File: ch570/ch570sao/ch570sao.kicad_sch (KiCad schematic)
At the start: 12 parts, among them J1 SAO, SW1 TS-1187A-B-A-B, SW2 TS-1187A-B-A-B, U2 CH570Q

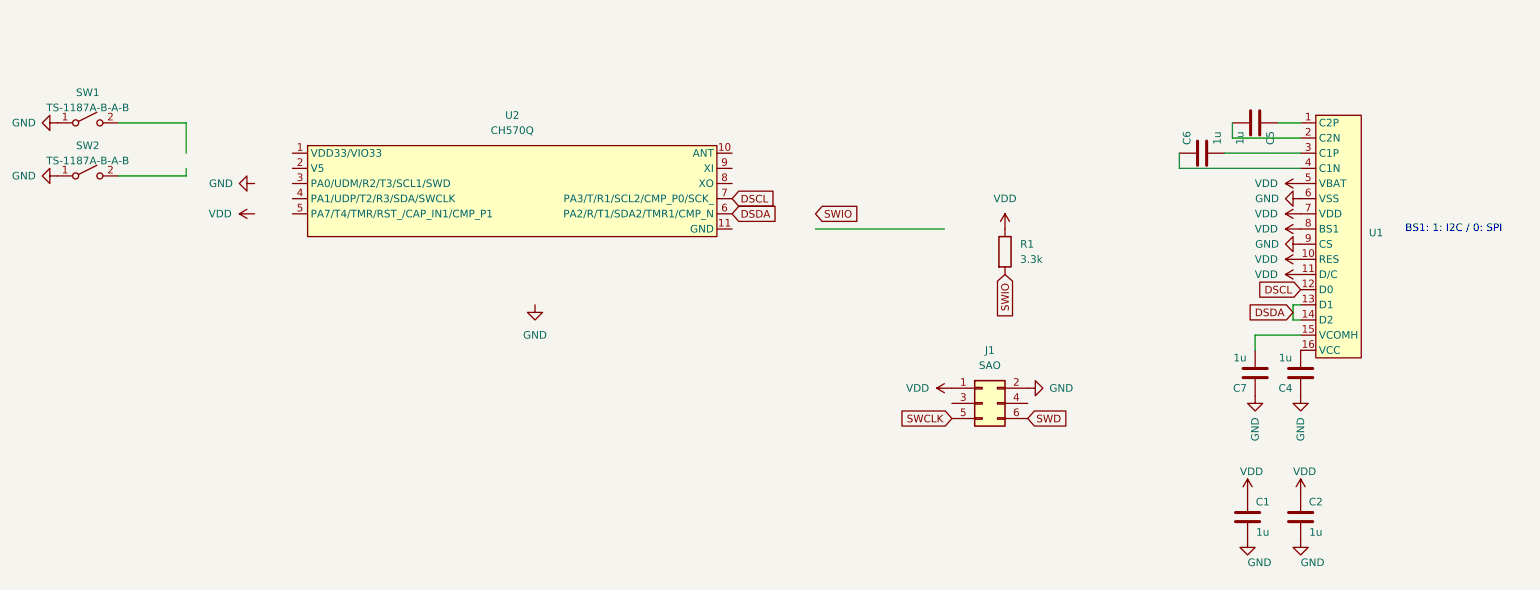
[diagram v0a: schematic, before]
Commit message: Add ch570 saob test
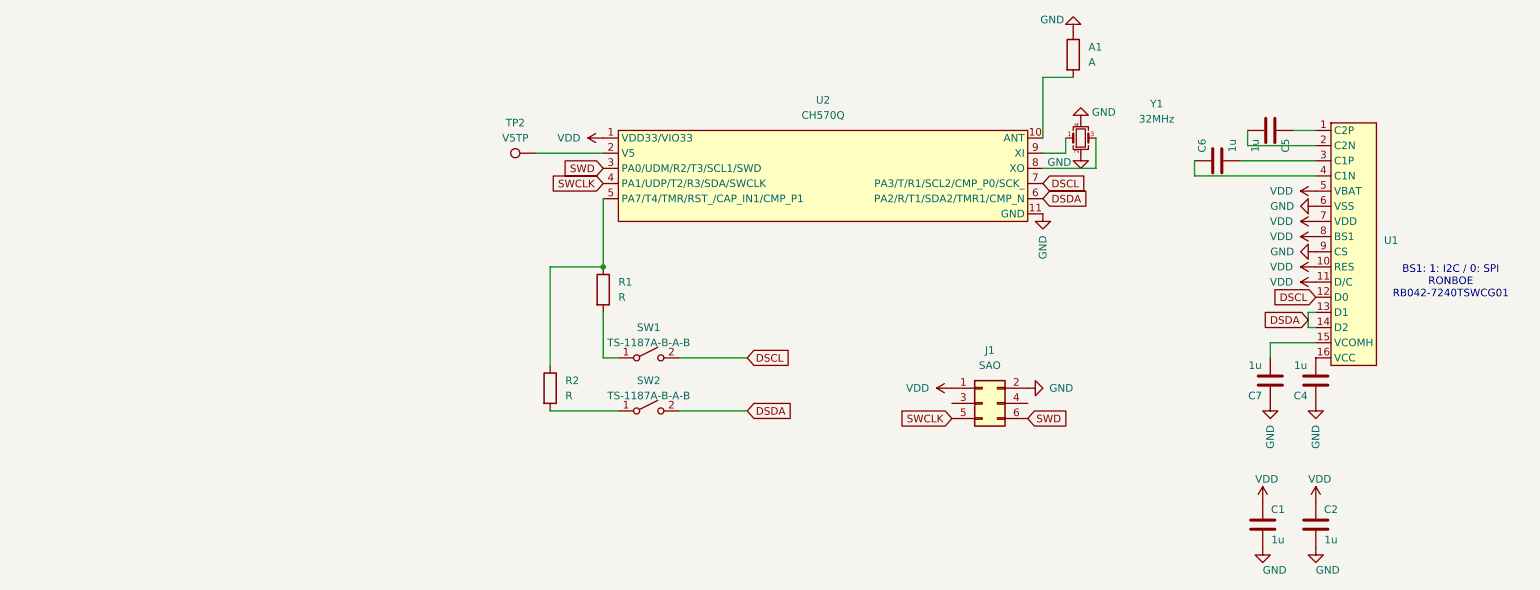
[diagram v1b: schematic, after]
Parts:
- added A1: A, RF_Antenna:Texas_SWRA117D_2.4GHz_Right, symbol Device:R
- added R2: R, Resistor_SMD:R_0402_1005Metric, symbol Device:R
- added TP2: V5TP, TestPoint:TestPoint_Pad_D1.0mm, symbol Connector:TestPoint
- added Y1: 32MHz, Crystal:Crystal_SMD_2016-4Pin_2.0x1.6mm, symbol Device:Crystal_GND24_Small
- R1: value 3.3k -> R; LCSC C25890 -> C25905
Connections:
- net DSCL: now also SW1.2 (B)
- net DSDA: now also SW2.2 (B)
- net GND: now also U2.11 (GND), A1.1, Y1.2, Y1.4; no longer SW1.1 (A), SW2.1 (A)
- net SWCLK: now also U2.4 (PA1/UDP/T2/R3/SDA/SWCLK)
- net SWD: now also U2.3 (PA0/UDM/R2/T3/SCL1/SWD)
- net VDD: now also U2.1 (VDD33/VIO33); no longer R1.1
- net at U2.10 (ANT): now also A1.2
- net at U2.2 (V5): now also TP2.1
- net at U2.5 (PA7/T4/TMR/RST_/CAP_IN1/CMP_P1): now also R1.1, R2.1
- net at U2.8 (XO): now also Y1.3
- net at U2.9 (XI): now also Y1.1
- net SWIO: no longer names the net of R1.2
- net SWIO: now also SW1.1 (A)
- new net: R2.2, SW2.1 (A)
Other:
- note added: "BS1: 1: I2C / 0: SPI RONBOE RB042-7240TSWCG01"
- note removed: "BS1: 1: I2C / 0: SPI"
- moved on the sheet: C1, C2, C4, C5, C6, C7, SW1, SW2, U1, U2

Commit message: Bump design
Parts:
- removed A1: A, RF_Antenna:Texas_SWRA117D_2.4GHz_Right, symbol Device:R
- R1, R2: value R -> 5.1k
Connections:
- net DSCL: now also R1.2; no longer SW1.2 (B)
- net DSDA: now also R2.2; no longer SW2.2 (B)
- net GND: now also U2.10 (ANT)
- net at SW2.1 (A): now also SW1.1 (A), U2.5 (PA7/T4/TMR/RST_/CAP_IN1/CMP_P1); no longer R2.2
- new net: R2.1, SW2.2 (B)
- new net: R1.1, SW1.2 (B)
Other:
- moved on the sheet: R1, R2
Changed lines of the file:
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@@
 	)
 	(junction
-		(at 115.57 62.23)
+		(at 115.57 77.47)
 		(diameter 0)
 		(color 0 0 0 0)
@@
 	(wire
 		(pts
-			(xy 189.23 30.48) (xy 194.31 30.48)
+			(xy 234.95 69.85) (xy 233.68 69.85)
 		)
 		(stroke
@@
 	(wire
 		(pts
-			(xy 234.95 69.85) (xy 233.68 69.85)
+			(xy 132.08 77.47) (xy 128.27 77.47)
 		)
 		(stroke
@@
 	(wire
 		(pts
-			(xy 139.7 77.47) (xy 128.27 77.47)
+			(xy 115.57 77.47) (xy 115.57 86.36)
 		)
 		(stroke
@@
 	(wire
 		(pts
-			(xy 115.57 62.23) (xy 115.57 50.8)
+			(xy 227.33 77.47) (xy 227.33 74.93)
 		)
 		(stroke
@@
 	(wire
 		(pts
-			(xy 227.33 77.47) (xy 227.33 74.93)
+			(xy 193.04 43.18) (xy 189.23 43.18)
 		)
 		(stroke
@@
 	(wire
 		(pts
-			(xy 193.04 43.18) (xy 189.23 43.18)
+			(xy 189.23 45.72) (xy 198.12 45.72)
 		)
 		(stroke
@@
 	(wire
 		(pts
-			(xy 189.23 45.72) (xy 198.12 45.72)
+			(xy 189.23 22.86) (xy 194.31 22.86)
 		)
 		(stroke
@@
 	(wire
 		(pts
-			(xy 106.68 62.23) (xy 115.57 62.23)
+			(xy 234.95 46.99) (xy 214.63 46.99)
 		)
 		(stroke
@@
 	(wire
 		(pts
-			(xy 234.95 46.99) (xy 214.63 46.99)
+			(xy 233.68 72.39) (xy 234.95 72.39)
 		)
 		(stroke
@@
 	(wire
 		(pts
-			(xy 106.68 78.74) (xy 106.68 62.23)
+			(xy 189.23 22.86) (xy 189.23 40.64)
 		)
 		(stroke
@@
 	(wire
 		(pts
-			(xy 128.27 86.36) (xy 139.7 86.36)
+			(xy 223.52 41.91) (xy 234.95 41.91)
 		)
 		(stroke
@@
 	(wire
 		(pts
-			(xy 233.68 72.39) (xy 234.95 72.39)
+			(xy 222.25 44.45) (xy 234.95 44.45)
 		)
 		(stroke
@@
 	(wire
 		(pts
-			(xy 189.23 40.64) (xy 189.23 30.48)
+			(xy 115.57 50.8) (xy 115.57 77.47)
 		)
 		(stroke
@@
 	(wire
 		(pts
-			(xy 223.52 41.91) (xy 234.95 41.91)
+			(xy 128.27 86.36) (xy 132.08 86.36)
 		)
 		(stroke
@@
 	(wire
 		(pts
-			(xy 115.57 77.47) (xy 115.57 69.85)
+			(xy 214.63 46.99) (xy 214.63 44.45)
 		)
 		(stroke
@@
 	(wire
 		(pts
-			(xy 222.25 44.45) (xy 234.95 44.45)
+			(xy 193.04 40.64) (xy 193.04 43.18)
 		)
 		(stroke
@@
 	(wire
 		(pts
-			(xy 214.63 46.99) (xy 214.63 44.45)
-		)
-		(stroke
-			(width 0)
-			(type default)
-		)
-	)
-	(wire
-		(pts
-			(xy 193.04 40.64) (xy 193.04 43.18)
-		)
-		(stroke
-			(width 0)
-			(type default)
-		)
-	)
-	(wire
-		(pts
-			(xy 106.68 86.36) (xy 118.11 86.36)
+			(xy 115.57 86.36) (xy 118.11 86.36)
 		)
 		(stroke
@@
 	(symbol
 		(lib_id "Device:R")
-		(at 106.68 82.55 0)
+		(at 135.89 86.36 90)
 		(unit 1)
 		(exclude_from_sim no)
@@
 		(fields_autoplaced yes)
 		(property "Reference" "R2"
-			(at 109.22 81.2799 0)
-			(effects
-				(font
-					(size 1.27 1.27)
-				)
-				(justify left)
-			)
-		)
-		(property "Value" "R"
-			(at 109.22 83.8199 0)
-			(effects
-				(font
-					(size 1.27 1.27)
-				)
-				(justify left)
+			(at 135.89 80.01 90)
+			(effects
+				(font
+					(size 1.27 1.27)
+				)
+			)
+		)
+		(property "Value" "5.1k"
+			(at 135.89 82.55 90)
+			(effects
+				(font
+					(size 1.27 1.27)
+				)
 			)
 		)
 		(property "Footprint" "Resistor_SMD:R_0402_1005Metric"
-			(at 104.902 82.55 90)
+			(at 135.89 88.138 90)
 			(effects
 				(font
@@
 		)
 		(property "Datasheet" "~"
-			(at 106.68 82.55 0)
+			(at 135.89 86.36 0)
 			(effects
 				(font
@@
 		)
 		(property "Description" "Resistor"
-			(at 106.68 82.55 0)
+			(at 135.89 86.36 0)
 			(effects
 				(font
@@
 		)
 		(property "LCSC" "C25905"
-			(at 106.68 82.55 0)
+			(at 135.89 86.36 0)
 			(effects
 				(font
@@
 	(symbol
 		(lib_id "Device:R")
-		(at 115.57 66.04 0)
+		(at 135.89 77.47 90)
 		(unit 1)
 		(exclude_from_sim no)
@@
 		(fields_autoplaced yes)
 		(property "Reference" "R1"
-			(at 118.11 64.7699 0)
-			(effects
-				(font
-					(size 1.27 1.27)
-				)
-				(justify left)
-			)
-		)
-		(property "Value" "R"
-			(at 118.11 67.3099 0)
-			(effects
-				(font
-					(size 1.27 1.27)
-				)
-				(justify left)
+			(at 135.89 71.12 90)
+			(effects
+				(font
+					(size 1.27 1.27)
+				)
+			)
+		)
+		(property "Value" "5.1k"
+			(at 135.89 73.66 90)
+			(effects
+				(font
+					(size 1.27 1.27)
+				)
 			)
 		)
 		(property "Footprint" "Resistor_SMD:R_0402_1005Metric"
-			(at 113.792 66.04 90)
+			(at 135.89 79.248 90)
 			(effects
 				(font
@@
 		)
 		(property "Datasheet" "~"
-			(at 115.57 66.04 0)
+			(at 135.89 77.47 0)
 			(effects
 				(font
@@
 		)
 		(property "Description" "Resistor"
-			(at 115.57 66.04 0)
+			(at 135.89 77.47 0)
 			(effects
 				(font
@@
 		)
 		(property "LCSC" "C25905"
-			(at 115.57 66.04 0)
+			(at 135.89 77.47 0)
 			(effects
 				(font
@@
 		)
 		(instances
-			(project ""
+			(project "ch570sao"
 				(path "/8b3ca9c1-ec01-472e-975f-b13c767b5c47"
 					(reference "R1")
@@
 					(unit 1)
 				)
-			)
-		)
-	)
-	(symbol
-		(lib_id "Device:R")
-		(at 194.31 26.67 0)
-		(unit 1)
-		(exclude_from_sim no)
-		(in_bom no)
-		(on_board yes)
-		(dnp no)
-		(fields_autoplaced yes)
-		(property "Reference" "A1"
-			(at 196.85 25.3999 0)
-			(effects
-				(font
-					(size 1.27 1.27)
-				)
-				(justify left)
-			)
-		)
-		(property "Value" "A"
-			(at 196.85 27.9399 0)
-			(effects
-				(font
-					(size 1.27 1.27)
-				)
-				(justify left)
-			)
-		)
-		(property "Footprint" "RF_Antenna:Texas_SWRA117D_2.4GHz_Right"
-			(at 192.532 26.67 90)
-			(effects
-				(font
-					(size 1.27 1.27)
-				)
-				(hide yes)
-			)
-		)
-		(property "Datasheet" "~"
-			(at 194.31 26.67 0)
-			(effects
-				(font
-					(size 1.27 1.27)
-				)
-				(hide yes)
-			)
-		)
-		(property "Description" "Resistor"
-			(at 194.31 26.67 0)
-			(effects
-				(font
-					(size 1.27 1.27)
-				)
-				(hide yes)
-			)
-		)
-		(pin "1"
-		)
-		(pin "2"
-		)
-		(instances
-			(project ""
-				(path "/8b3ca9c1-ec01-472e-975f-b13c767b5c47"
-					(reference "A1")
-					(unit 1)
-				)
